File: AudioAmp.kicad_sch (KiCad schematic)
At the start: 56 parts, among them J1 ACJS-MHOM, J2 ACJS-MHOM, Q1 MJE182G, Q12 MMBT5401, Q13 MMBT5401, Q2 MJE172G, Q3 MMBT5551(RANGE:200-300), Q9 MMBT5551(RANGE:200-300)

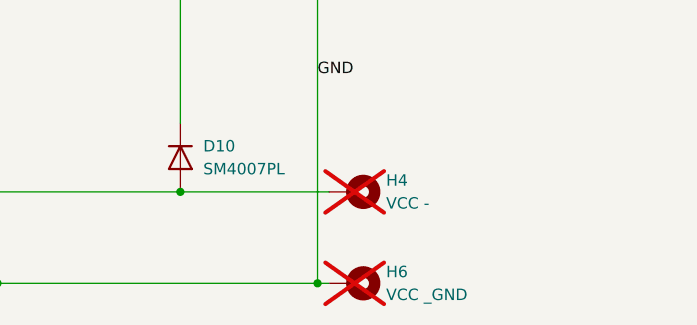
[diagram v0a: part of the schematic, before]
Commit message: CHA: Testpin zu Points
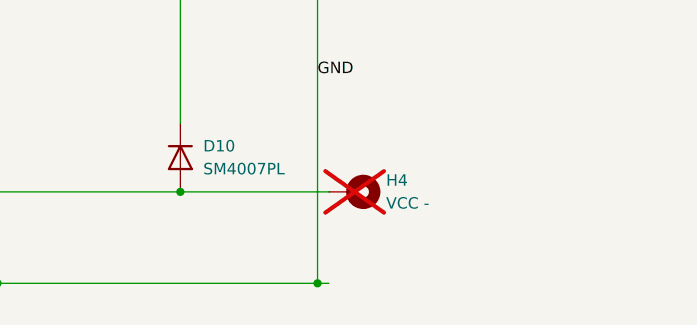
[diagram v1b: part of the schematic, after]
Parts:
- removed H6: VCC _GND, MountingHole:MountingHole_2.5mm_Pad, symbol Mechanical:MountingHole_Pad
- TP1, TP10, TP2, TP3, TP4, TP5, TP6, TP7, TP8, TP9: footprint Connector_Pin:Pin_D1.0mm_L10.0mm -> TestPoint:TestPoint_Pad_1.0x1.0mm
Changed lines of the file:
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@@
 			)
 		)
-		(property "Footprint" "Connector_Pin:Pin_D1.0mm_L10.0mm"
+		(property "Footprint" "TestPoint:TestPoint_Pad_1.0x1.0mm"
 			(at 130.81 77.47 0)
 			(effects
@@
 			)
 		)
-		(property "Footprint" "Connector_Pin:Pin_D1.0mm_L10.0mm"
+		(property "Footprint" "TestPoint:TestPoint_Pad_1.0x1.0mm"
 			(at 137.16 138.43 0)
 			(effects
@@
 			)
 		)
-		(property "Footprint" "Connector_Pin:Pin_D1.0mm_L10.0mm"
+		(property "Footprint" "TestPoint:TestPoint_Pad_1.0x1.0mm"
 			(at 137.16 128.27 0)
 			(effects
@@
 	(symbol
 		(lib_id "Mechanical:MountingHole_Pad")
-		(at 261.62 138.43 270)
-		(unit 1)
-		(exclude_from_sim no)
-		(in_bom no)
-		(on_board yes)
-		(dnp yes)
-		(fields_autoplaced yes)
-		(property "Reference" "H6"
-			(at 265.43 137.1599 90)
-			(effects
-				(font
-					(size 1.27 1.27)
-				)
-				(justify left)
-			)
-		)
-		(property "Value" "VCC _GND"
-			(at 265.43 139.6999 90)
-			(effects
-				(font
-					(size 1.27 1.27)
-				)
-				(justify left)
-			)
-		)
-		(property "Footprint" "MountingHole:MountingHole_2.5mm_Pad"
-			(at 261.62 138.43 0)
-			(effects
-				(font
-					(size 1.27 1.27)
-				)
-				(hide yes)
-			)
-		)
-		(property "Datasheet" "~"
-			(at 261.62 138.43 0)
-			(effects
-				(font
-					(size 1.27 1.27)
-				)
-				(hide yes)
-			)
-		)
-		(property "Description" "Mounting Hole with connection"
-			(at 261.62 138.43 0)
-			(effects
-				(font
-					(size 1.27 1.27)
-				)
-				(hide yes)
-			)
-		)
-		(pin "1"
-		)
-		(instances
-			(project ""
-				(path "/c5a26e6d-aabf-49ab-a44e-c2ec87fd373d"
-					(reference "H6")
-					(unit 1)
-				)
-			)
-		)
-	)
-	(symbol
-		(lib_id "Mechanical:MountingHole_Pad")
 		(at 261.62 50.8 270)
 		(unit 1)
@@
 			)
 		)
-		(property "Footprint" "Connector_Pin:Pin_D1.0mm_L10.0mm"
+		(property "Footprint" "TestPoint:TestPoint_Pad_1.0x1.0mm"
 			(at 212.09 73.66 0)
 			(effects
@@
 			)
 		)
-		(property "Footprint" "Connector_Pin:Pin_D1.0mm_L10.0mm"
+		(property "Footprint" "TestPoint:TestPoint_Pad_1.0x1.0mm"
 			(at 99.06 77.47 0)
 			(effects
@@
 			)
 		)
-		(property "Footprint" "Connector_Pin:Pin_D1.0mm_L10.0mm"
+		(property "Footprint" "TestPoint:TestPoint_Pad_1.0x1.0mm"
 			(at 138.43 111.76 0)
 			(effects
@@
 			)
 		)
-		(property "Footprint" "Connector_Pin:Pin_D1.0mm_L10.0mm"
+		(property "Footprint" "TestPoint:TestPoint_Pad_1.0x1.0mm"
 			(at 116.84 50.8 0)
 			(effects
@@
 			)
 		)
-		(property "Footprint" "Connector_Pin:Pin_D1.0mm_L10.0mm"
+		(property "Footprint" "TestPoint:TestPoint_Pad_1.0x1.0mm"
 			(at 171.45 86.36 0)
 			(effects
@@
 			)
 		)
-		(property "Footprint" "Connector_Pin:Pin_D1.0mm_L10.0mm"
+		(property "Footprint" "TestPoint:TestPoint_Pad_1.0x1.0mm"
 			(at 210.82 100.33 0)
 			(effects
@@
 			)
 		)
-		(property "Footprint" "Connector_Pin:Pin_D1.0mm_L10.0mm"
+		(property "Footprint" "TestPoint:TestPoint_Pad_1.0x1.0mm"
 			(at 232.41 78.74 0)
 			(effects

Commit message: CHA: MPN bei den Testpoints raus
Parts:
- TP1, TP10, TP2, TP3, TP4, TP5, TP6, TP7, TP8, TP9: MPN C9900045500 -> (none)
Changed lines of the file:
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@@
 			)
 		)
-		(property "MPN" "C9900045500"
-			(at 125.73 77.47 0)
-			(effects
-				(font
-					(size 1.27 1.27)
-				)
-				(hide yes)
-			)
-		)
 		(pin "1"
 		)
@@
 			)
 		)
-		(property "MPN" "C9900045500"
-			(at 132.08 138.43 0)
-			(effects
-				(font
-					(size 1.27 1.27)
-				)
-				(hide yes)
-			)
-		)
 		(pin "1"
 		)
@@
 			)
 		)
-		(property "MPN" "C9900045500"
-			(at 132.08 128.27 0)
-			(effects
-				(font
-					(size 1.27 1.27)
-				)
-				(hide yes)
-			)
-		)
 		(pin "1"
 		)
@@
 			)
 		)
-		(property "MPN" "C9900045500"
-			(at 212.09 68.58 90)
-			(effects
-				(font
-					(size 1.27 1.27)
-				)
-				(hide yes)
-			)
-		)
 		(pin "1"
 		)
@@
 			)
 		)
-		(property "MPN" "C9900045500"
-			(at 93.98 77.47 0)
-			(effects
-				(font
-					(size 1.27 1.27)
-				)
-				(hide yes)
-			)
-		)
 		(pin "1"
 		)
@@
 			)
 		)
-		(property "MPN" "C9900045500"
-			(at 133.35 111.76 0)
-			(effects
-				(font
-					(size 1.27 1.27)
-				)
-				(hide yes)
-			)
-		)
 		(pin "1"
 		)
@@
 			)
 		)
-		(property "MPN" "C9900045500"
-			(at 111.76 50.8 0)
-			(effects
-				(font
-					(size 1.27 1.27)
-				)
-				(hide yes)
-			)
-		)
 		(pin "1"
 		)
@@
 			)
 		)
-		(property "MPN" "C9900045500"
-			(at 171.45 91.44 90)
-			(effects
-				(font
-					(size 1.27 1.27)
-				)
-				(hide yes)
-			)
-		)
 		(pin "1"
 		)
@@
 			)
 		)
-		(property "MPN" "C9900045500"
-			(at 210.82 95.25 90)
-			(effects
-				(font
-					(size 1.27 1.27)
-				)
-				(hide yes)
-			)
-		)
 		(pin "1"
 		)
@@
 			(at 227.33 78.74 0)
 			(effects
-				(font
-					(size 1.27 1.27)
-				)
-				(hide yes)
-			)
-		)
-		(property "MPN" "C9900045500"
-			(at 227.33 78.74 0)
-			(effects

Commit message: CHA: Tp auf 2mm
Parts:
- TP1, TP10, TP2, TP3, TP4, TP5, TP6, TP7, TP8, TP9: footprint TestPoint:TestPoint_Pad_1.0x1.0mm -> TestPoint:TestPoint_Pad_2.0x2.0mm
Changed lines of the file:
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@@
 			)
 		)
-		(property "Footprint" "TestPoint:TestPoint_Pad_1.0x1.0mm"
+		(property "Footprint" "TestPoint:TestPoint_Pad_2.0x2.0mm"
 			(at 130.81 77.47 0)
 			(effects
@@
 			)
 		)
-		(property "Footprint" "TestPoint:TestPoint_Pad_1.0x1.0mm"
+		(property "Footprint" "TestPoint:TestPoint_Pad_2.0x2.0mm"
 			(at 137.16 138.43 0)
 			(effects
@@
 			)
 		)
-		(property "Footprint" "TestPoint:TestPoint_Pad_1.0x1.0mm"
+		(property "Footprint" "TestPoint:TestPoint_Pad_2.0x2.0mm"
 			(at 137.16 128.27 0)
 			(effects
@@
 			)
 		)
-		(property "Footprint" "TestPoint:TestPoint_Pad_1.0x1.0mm"
+		(property "Footprint" "TestPoint:TestPoint_Pad_2.0x2.0mm"
 			(at 212.09 73.66 0)
 			(effects
@@
 			)
 		)
-		(property "Footprint" "TestPoint:TestPoint_Pad_1.0x1.0mm"
+		(property "Footprint" "TestPoint:TestPoint_Pad_2.0x2.0mm"
 			(at 99.06 77.47 0)
 			(effects
@@
 			)
 		)
-		(property "Footprint" "TestPoint:TestPoint_Pad_1.0x1.0mm"
+		(property "Footprint" "TestPoint:TestPoint_Pad_2.0x2.0mm"
 			(at 138.43 111.76 0)
 			(effects
@@
 			)
 		)
-		(property "Footprint" "TestPoint:TestPoint_Pad_1.0x1.0mm"
+		(property "Footprint" "TestPoint:TestPoint_Pad_2.0x2.0mm"
 			(at 116.84 50.8 0)
 			(effects
@@
 			)
 		)
-		(property "Footprint" "TestPoint:TestPoint_Pad_1.0x1.0mm"
+		(property "Footprint" "TestPoint:TestPoint_Pad_2.0x2.0mm"
 			(at 171.45 86.36 0)
 			(effects
@@
 			)
 		)
-		(property "Footprint" "TestPoint:TestPoint_Pad_1.0x1.0mm"
+		(property "Footprint" "TestPoint:TestPoint_Pad_2.0x2.0mm"
 			(at 210.82 100.33 0)
 			(effects
@@
 			)
 		)
-		(property "Footprint" "TestPoint:TestPoint_Pad_1.0x1.0mm"
+		(property "Footprint" "TestPoint:TestPoint_Pad_2.0x2.0mm"
 			(at 232.41 78.74 0)
 			(effects

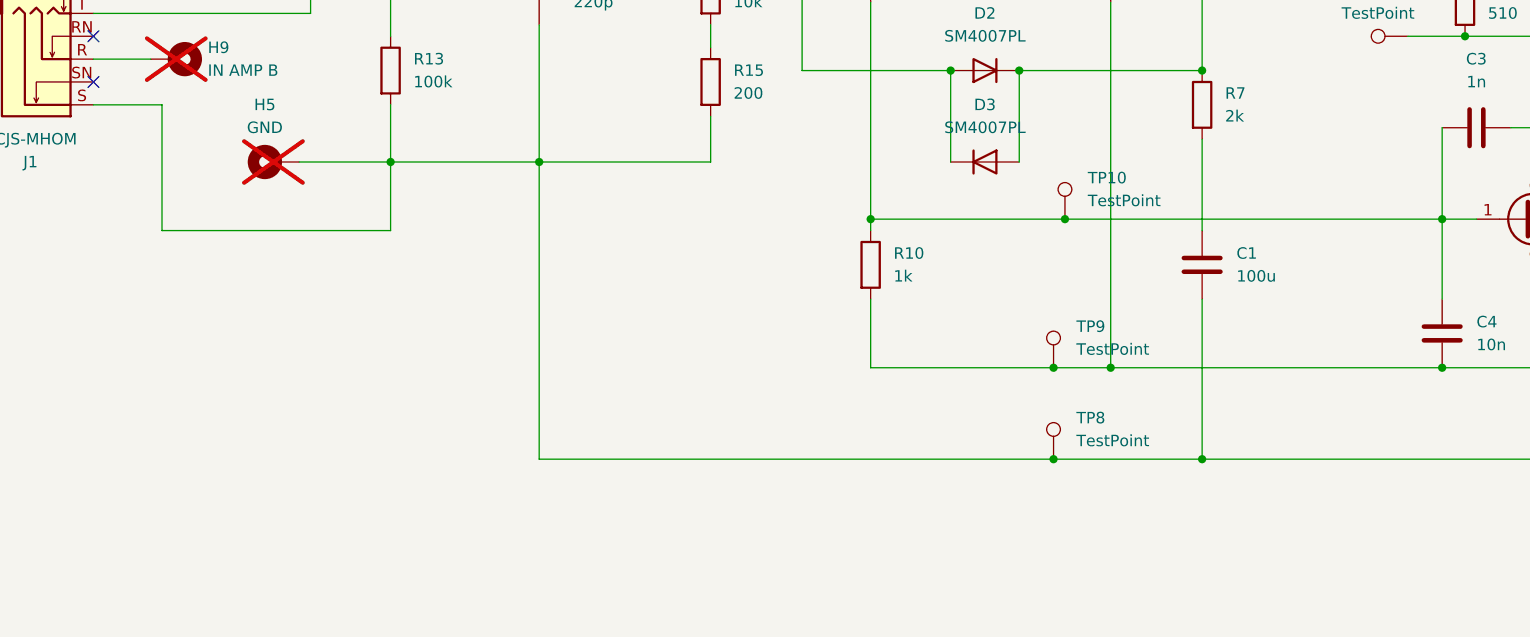
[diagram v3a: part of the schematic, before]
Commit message: CHA: Testpads, leitungsänderungen
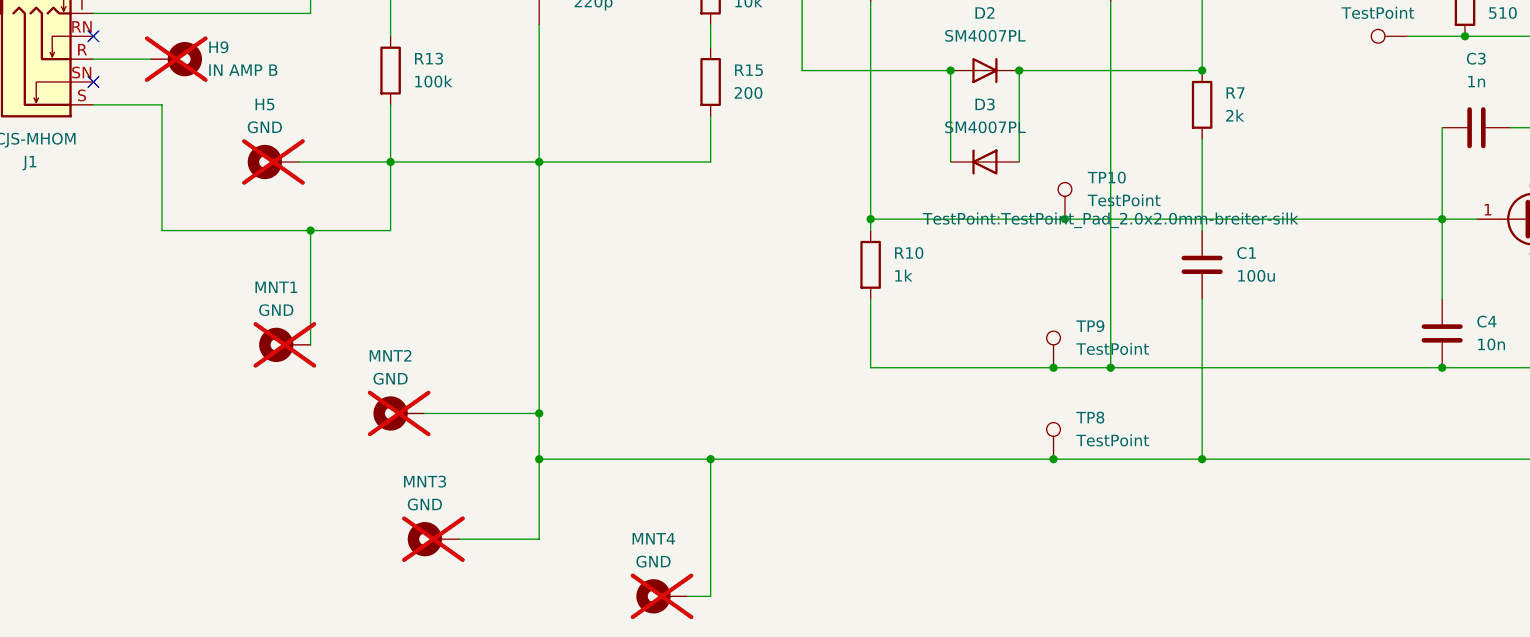
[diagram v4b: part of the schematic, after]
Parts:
- added MNT1, MNT2, MNT3, MNT4: GND, MountingHole:MountingHole_2.5mm_Pad, symbol Mechanical:MountingHole_Pad
- TP1, TP10, TP2, TP3, TP4, TP5, TP6, TP7, TP8, TP9: footprint TestPoint:TestPoint_Pad_2.0x2.0mm -> TestPoint:TestPoint_Pad_2.0x2.0mm-breiter-silk
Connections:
- net GND: now also MNT1.1, MNT2.1, MNT3.1, MNT4.1
